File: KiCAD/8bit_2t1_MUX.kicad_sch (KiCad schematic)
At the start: 2 parts, among them U55 74HC257, U56 74HC257

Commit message: finished schematics and footprint assignments; need to figure out +5v connection issue
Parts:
- U37: renamed from U55; footprint (none) -> Package_DIP:DIP-16_W7.62mm
- U38: renamed from U56; footprint (none) -> Package_DIP:DIP-16_W7.62mm
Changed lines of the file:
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@@
 		(dnp no)
 		(fields_autoplaced yes)
-		(property "Reference" "U56"
+		(property "Reference" "U38"
 			(at 132.9533 62.23 0)
 			(effects
@@
 			)
 		)
-		(property "Footprint" ""
+		(property "Footprint" "Package_DIP:DIP-16_W7.62mm"
 			(at 130.81 85.09 0)
 			(effects
@@
 		(instances
 			(project "vga_video_card"
+				(path "/53ebbfbe-eaa1-4706-acc1-611a99db7179/c08e26f6-31d4-4f9e-9b0c-128d1955ff42/8ec64eda-b8f0-452c-8446-121b177053a7"
+					(reference "U38")
+					(unit 1)
+				)
 				(path "/53ebbfbe-eaa1-4706-acc1-611a99db7179/a295050b-d209-4efc-8327-c0e97d5127bf/9d9429b1-c4f4-4d06-b7d7-8f5f8e69e70c/e9943e04-24d6-4469-9ff0-37b964b5055b"
 					(reference "U56")
@@
 		(dnp no)
 		(fields_autoplaced yes)
-		(property "Reference" "U55"
+		(property "Reference" "U37"
 			(at 92.3133 62.23 0)
 			(effects
@@
 			)
 		)
-		(property "Footprint" ""
+		(property "Footprint" "Package_DIP:DIP-16_W7.62mm"
 			(at 90.17 85.09 0)
 			(effects
@@
 		(instances
 			(project "vga_video_card"
+				(path "/53ebbfbe-eaa1-4706-acc1-611a99db7179/c08e26f6-31d4-4f9e-9b0c-128d1955ff42/8ec64eda-b8f0-452c-8446-121b177053a7"
+					(reference "U37")
+					(unit 1)
+				)
 				(path "/53ebbfbe-eaa1-4706-acc1-611a99db7179/a295050b-d209-4efc-8327-c0e97d5127bf/9d9429b1-c4f4-4d06-b7d7-8f5f8e69e70c/e9943e04-24d6-4469-9ff0-37b964b5055b"
 					(reference "U55")
@@
 		(dnp no)
 		(fields_autoplaced yes)
-		(property "Reference" "#PWR0117"
+		(property "Reference" "#PWR0104"
 			(at 90.17 116.84 0)
 			(effects
@@
 		(instances
 			(project "vga_video_card"
+				(path "/53ebbfbe-eaa1-4706-acc1-611a99db7179/c08e26f6-31d4-4f9e-9b0c-128d1955ff42/8ec64eda-b8f0-452c-8446-121b177053a7"
+					(reference "#PWR0104")
+					(unit 1)
+				)
 				(path "/53ebbfbe-eaa1-4706-acc1-611a99db7179/a295050b-d209-4efc-8327-c0e97d5127bf/9d9429b1-c4f4-4d06-b7d7-8f5f8e69e70c/e9943e04-24d6-4469-9ff0-37b964b5055b"
 					(reference "#PWR0117")
@@
 		(dnp no)
 		(fields_autoplaced yes)
-		(property "Reference" "#PWR0116"
+		(property "Reference" "#PWR0103"
 			(at 90.17 66.04 0)
 			(effects
@@
 		(instances
 			(project "vga_video_card"
+				(path "/53ebbfbe-eaa1-4706-acc1-611a99db7179/c08e26f6-31d4-4f9e-9b0c-128d1955ff42/8ec64eda-b8f0-452c-8446-121b177053a7"
+					(reference "#PWR0103")
+					(unit 1)
+				)
 				(path "/53ebbfbe-eaa1-4706-acc1-611a99db7179/a295050b-d209-4efc-8327-c0e97d5127bf/9d9429b1-c4f4-4d06-b7d7-8f5f8e69e70c/e9943e04-24d6-4469-9ff0-37b964b5055b"
 					(reference "#PWR0116")

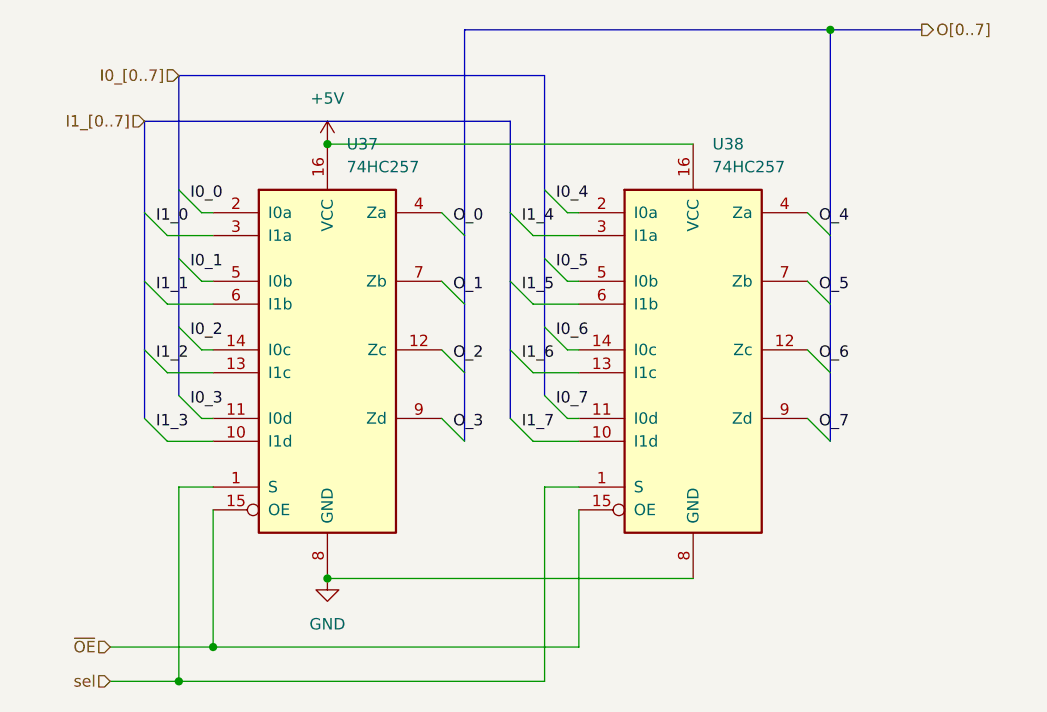
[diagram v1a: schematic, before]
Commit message: fix multiple ERCs that made RAM addrs not connecting
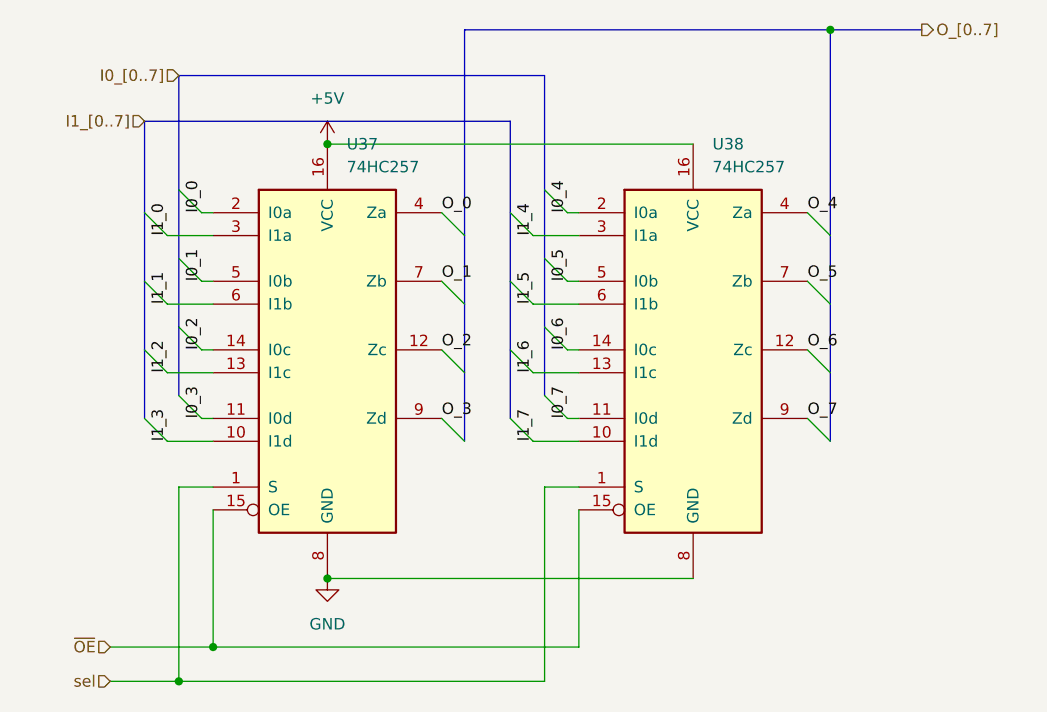
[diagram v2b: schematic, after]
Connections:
- net I0_0: now also U37.2 (I0a)
- net I0_1: now also U37.5 (I0b)
- net I0_2: now also U37.14 (I0c)
- net I0_3: now also U37.11 (I0d)
- net I0_4: now also U38.2 (I0a)
- net I0_5: now also U38.5 (I0b)
- net I0_6: now also U38.14 (I0c)
- net I0_7: now also U38.11 (I0d)
- net I1_0: now also U37.3 (I1a)
- net I1_1: now also U37.6 (I1b)
- net I1_2: now also U37.13 (I1c)
- net I1_3: now also U37.10 (I1d)
- net I1_4: now also U38.3 (I1a)
- net I1_5: now also U38.6 (I1b)
- net I1_6: now also U38.13 (I1c)
- net I1_7: now also U38.10 (I1d)
- net O_0: now also U37.4 (Za)
- net O_1: now also U37.7 (Zb)
- net O_2: now also U37.12 (Zc)
- net O_3: now also U37.9 (Zd)
- net O_4: now also U38.4 (Za)
- net O_5: now also U38.7 (Zb)
- net O_6: now also U38.12 (Zc)
- net O_7: now also U38.9 (Zd)
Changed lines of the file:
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@@
 	)
 	(label "I1_0"
-		(at 71.12 71.12 0)
+		(at 72.39 72.39 90)
 		(effects
 			(font
@@
 	)
 	(label "I1_6"
-		(at 111.76 86.36 0)
+		(at 113.03 87.63 90)
 		(effects
 			(font
@@
 	)
 	(label "O_7"
-		(at 144.78 93.98 0)
+		(at 143.51 92.71 0)
 		(effects
 			(font
@@
 	)
 	(label "I0_6"
-		(at 115.57 83.82 0)
+		(at 116.84 85.09 90)
 		(effects
 			(font
@@
 	)
 	(label "O_6"
-		(at 144.78 86.36 0)
+		(at 143.51 85.09 0)
 		(effects
 			(font
@@
 	)
 	(label "I0_7"
-		(at 115.57 91.44 0)
+		(at 116.84 92.71 90)
 		(effects
 			(font
@@
 	)
 	(label "I1_4"
-		(at 111.76 71.12 0)
+		(at 113.03 72.39 90)
 		(effects
 			(font
@@
 	)
 	(label "I1_5"
-		(at 111.76 78.74 0)
+		(at 113.03 80.01 90)
 		(effects
 			(font
@@
 	)
 	(label "I0_3"
-		(at 74.93 91.44 0)
+		(at 76.2 92.71 90)
 		(effects
 			(font
@@
 	)
 	(label "I1_3"
-		(at 71.12 93.98 0)
+		(at 72.39 95.25 90)
 		(effects
 			(font
@@
 	)
 	(label "O_4"
-		(at 144.78 71.12 0)
+		(at 143.51 69.85 0)
 		(effects
 			(font
@@
 	)
 	(label "O_5"
-		(at 144.78 78.74 0)
+		(at 143.51 77.47 0)
 		(effects
 			(font
@@
 	)
 	(label "O_0"
-		(at 104.14 71.12 0)
+		(at 102.87 69.85 0)
 		(effects
 			(font
@@
 	)
 	(label "O_1"
-		(at 104.14 78.74 0)
+		(at 102.87 77.47 0)
 		(effects
 			(font
@@
 	)
 	(label "O_2"
-		(at 104.14 86.36 0)
+		(at 102.87 85.09 0)
 		(effects
 			(font
@@
 	)
 	(label "I0_1"
-		(at 74.93 76.2 0)
+		(at 76.2 77.47 90)
 		(effects
 			(font
@@
 	)
 	(label "I1_2"
-		(at 71.12 86.36 0)
+		(at 72.39 87.63 90)
 		(effects
 			(font
@@
 	)
 	(label "I1_1"
-		(at 71.12 78.74 0)
+		(at 72.39 80.01 90)
 		(effects
 			(font
@@
 	)
 	(label "I0_2"
-		(at 74.93 83.82 0)
+		(at 76.2 85.09 90)
 		(effects
 			(font
@@
 	)
 	(label "I0_5"
-		(at 115.57 76.2 0)
+		(at 116.84 77.47 90)
 		(effects
 			(font
@@
 	)
 	(label "I1_7"
-		(at 111.76 93.98 0)
+		(at 113.03 95.25 90)
 		(effects
 			(font
@@
 	)
 	(label "I0_0"
-		(at 74.93 68.58 0)
+		(at 76.2 69.85 90)
 		(effects
 			(font
@@
 	)
 	(label "I0_4"
-		(at 115.57 68.58 0)
+		(at 116.84 69.85 90)
 		(effects
 			(font
@@
 	)
 	(label "O_3"
-		(at 104.14 93.98 0)
+		(at 102.87 92.71 0)
 		(effects
 			(font
@@
 		)
 	)
-	(hierarchical_label "O[0..7]"
+	(hierarchical_label "O_[0..7]"
 		(shape output)
 		(at 156.21 49.53 0)
